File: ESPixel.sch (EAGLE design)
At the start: 15 parts, among them Q1 MOSFET-NCHANNEL2N7000

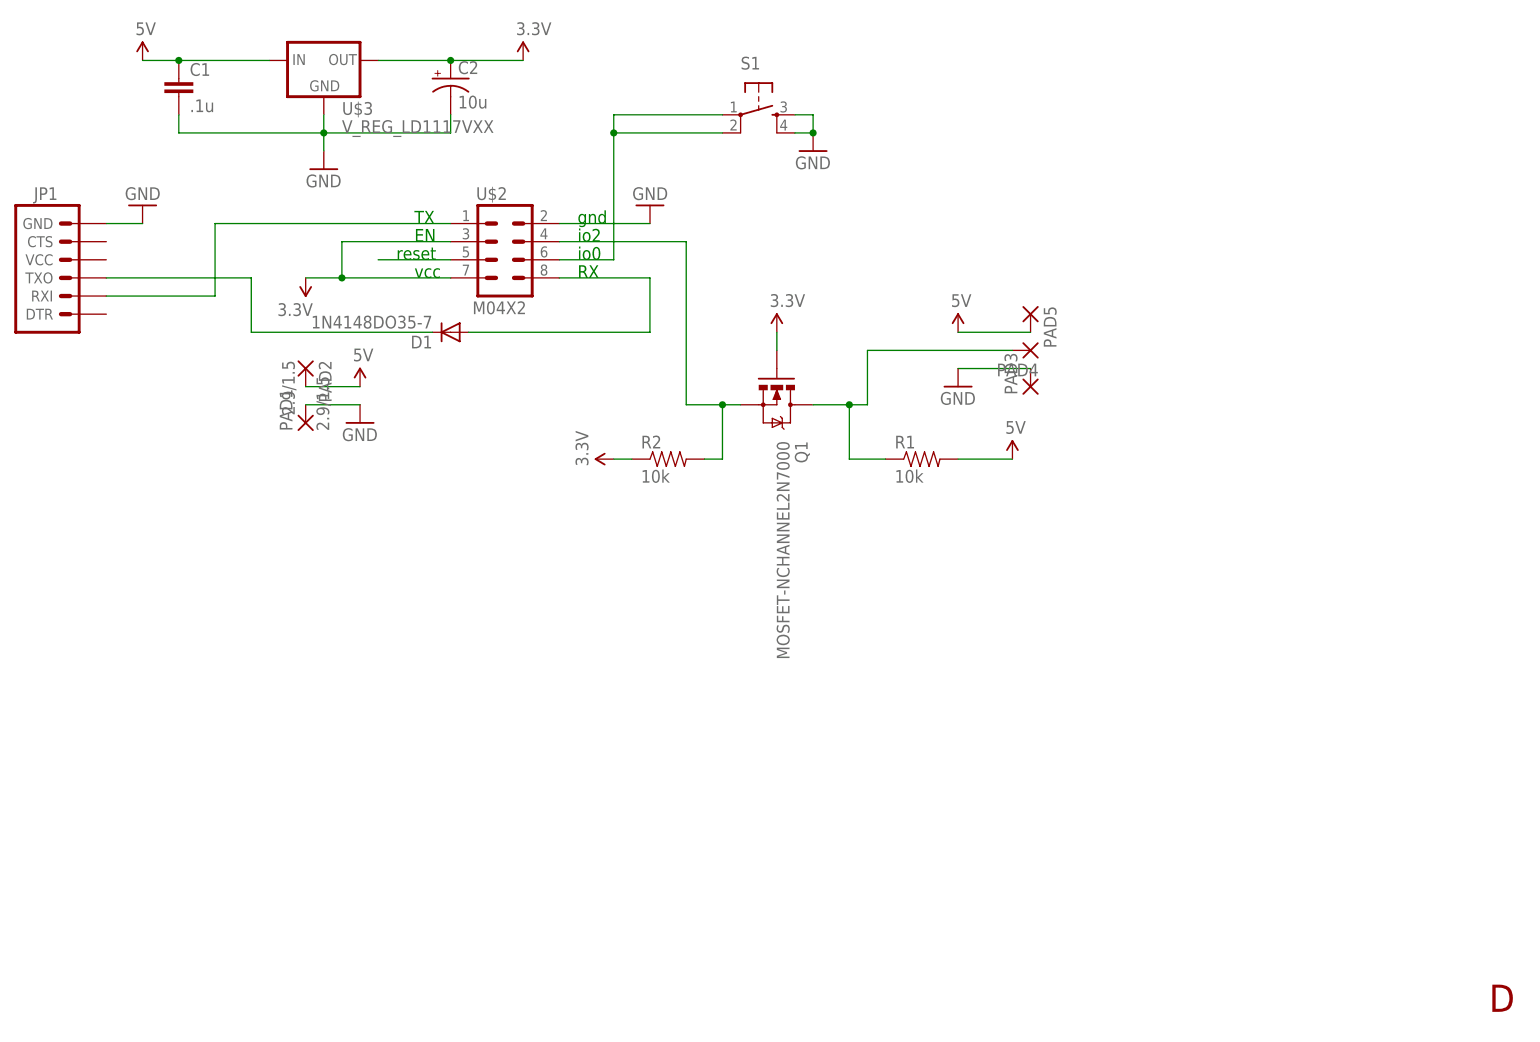
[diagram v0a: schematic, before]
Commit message: Added Diode to GECE and added WS2811 version
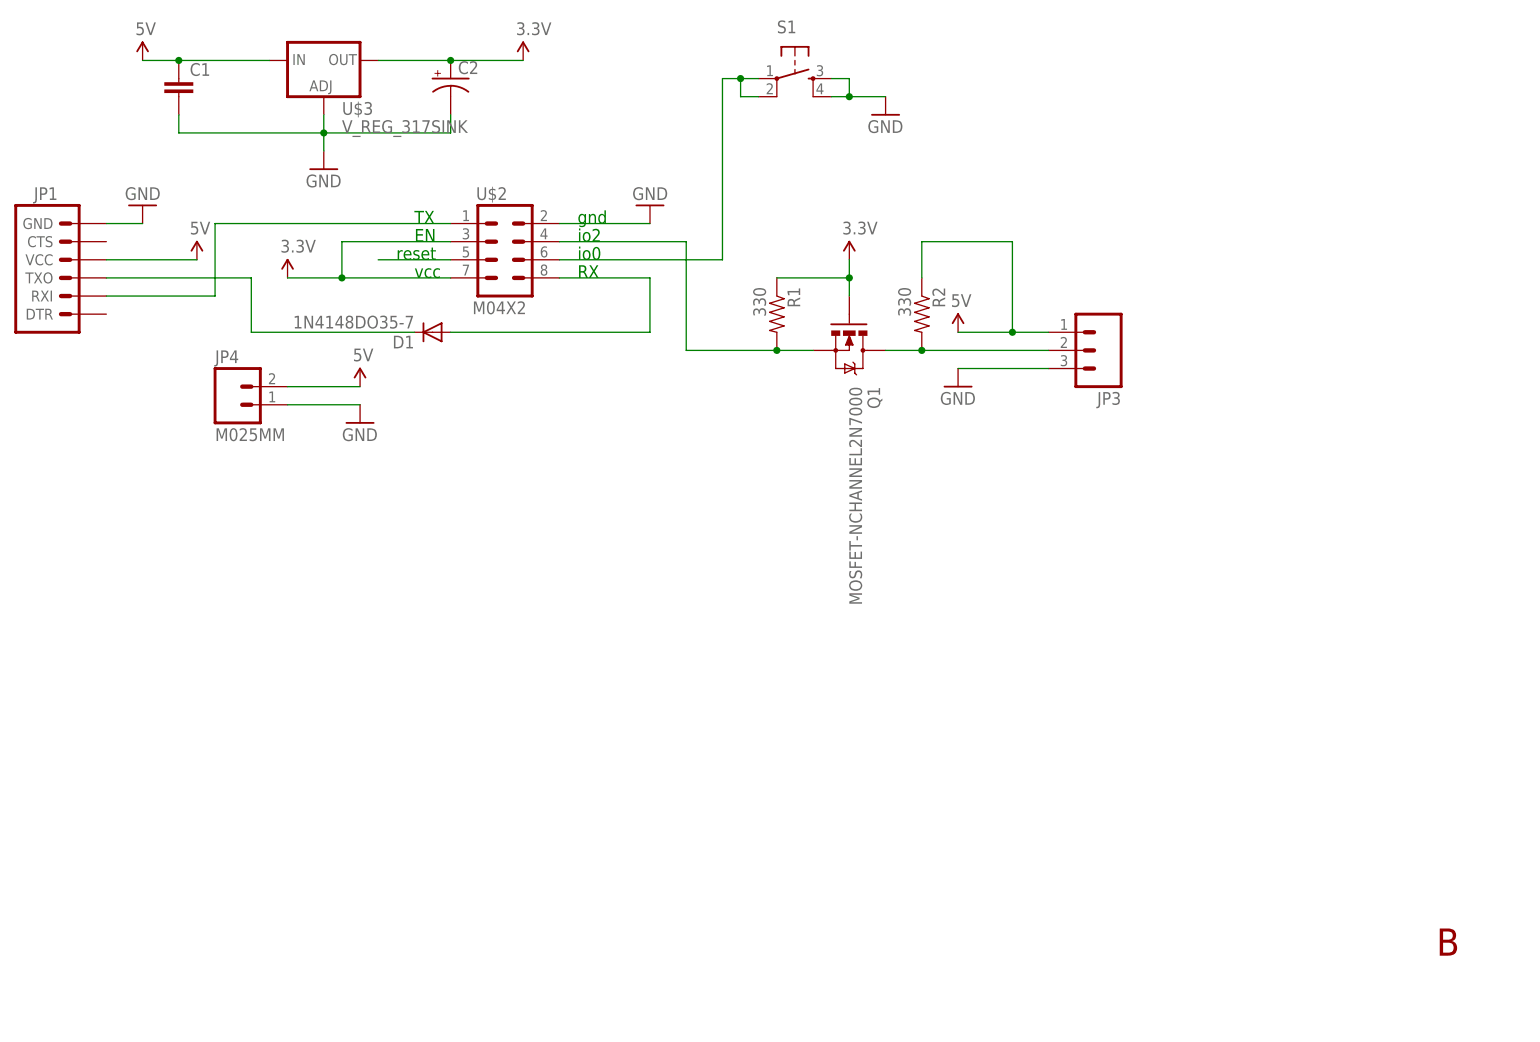
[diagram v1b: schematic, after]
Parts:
- removed PAD1, PAD2: 2.9/1.5, wirepad:2.9/1.5
- removed PAD3, PAD4, PAD5: (no value), wirepad:2,15/1,0
- added JP3: (no value), SparkFun-Connectors:M03-SCREW-5MM
- added JP4: M025MM, SparkFun-Connectors:M025MM
- C1: value .1u -> (none)
- C2: value 10u -> (none)
- R1, R2: value 10k -> 330
- U$3: value V_REG_LD1117VXX -> V_REG_317SINK; device SparkFun-PowerIC:V_REG_LD1117VXX -> SparkFun-PowerIC:V_REG_317SINK
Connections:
- net 3.3V: now also R1.1; no longer R2.1
- net 5V: now also JP1.VCC, JP3.1, JP4.2, R2.1; no longer PAD2.P, PAD5.P, R1.2
- net GND: now also JP3.3, JP4.1, U$3.ADJ; no longer PAD1.P, PAD3.P, U$3.GND
- net N$4: now also JP3.2, R2.2; no longer PAD4.P, R1.1
- net N$6: now also R1.2; no longer R2.2
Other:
- note added: "B"
- note removed: "D"
- moved on the sheet: D1, Q1, R1, R2, S1

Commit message: ESPixel now 12V or 5V
Added 5V reg for 12V pixel operation.
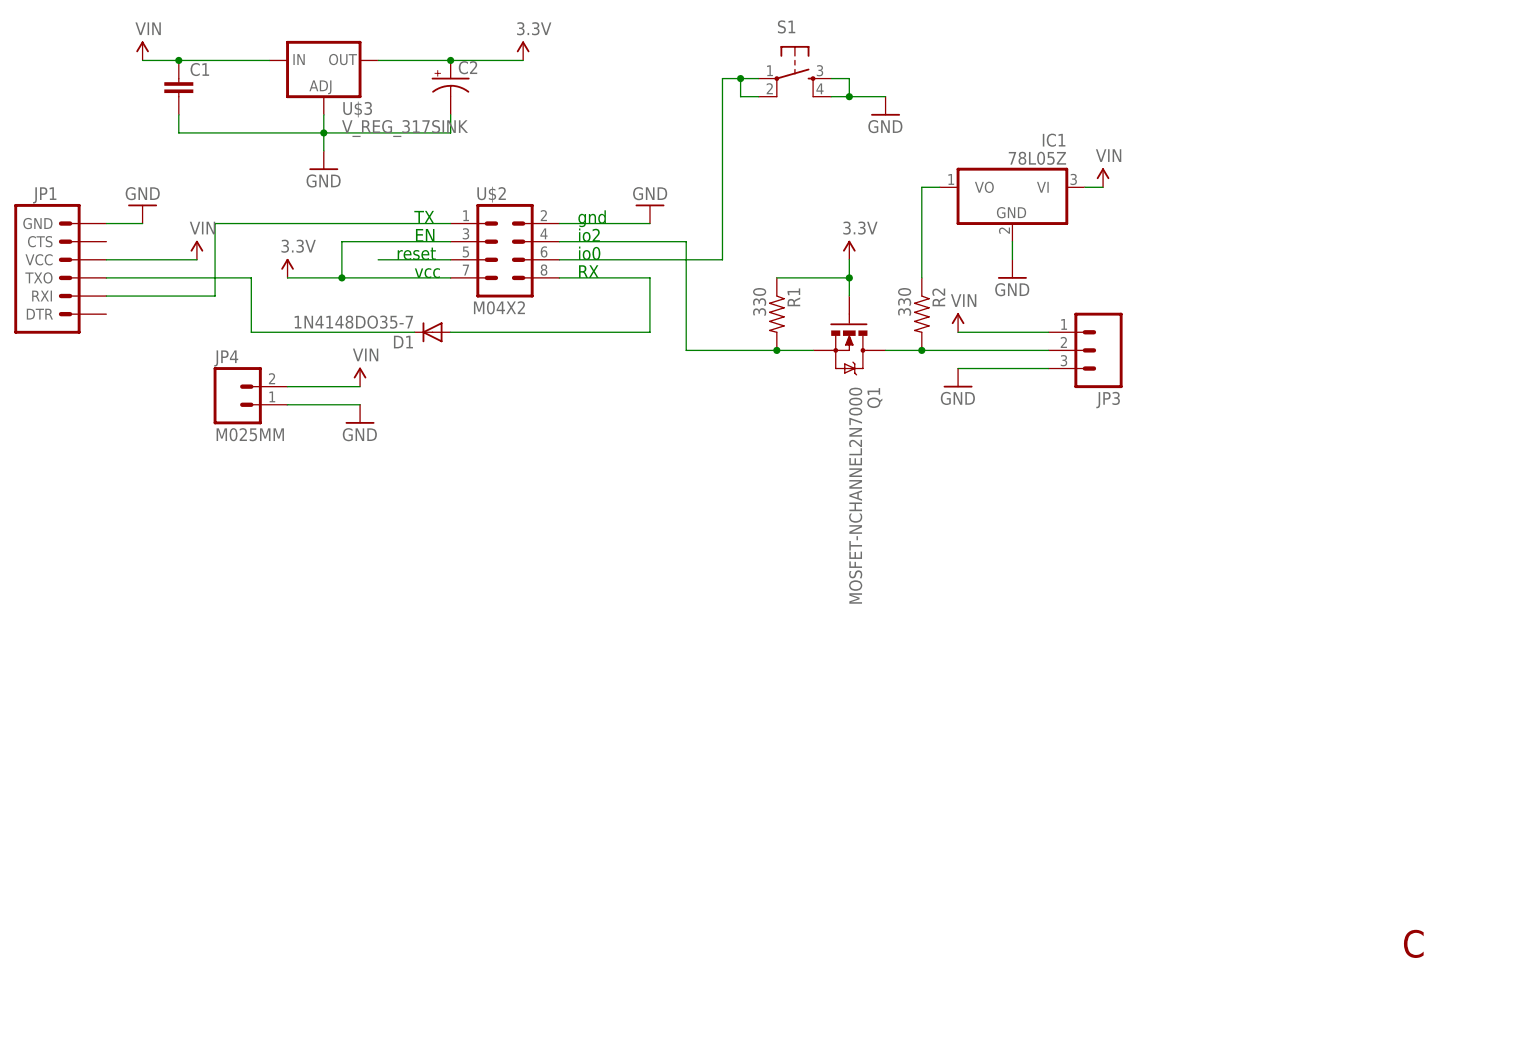
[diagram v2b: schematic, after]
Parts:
- added IC1: 78L05Z, linear:78L05Z
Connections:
- removed net 5V: C1.1, JP1.VCC, JP3.1, JP4.2, R2.1, U$3.IN
- new net N$2: IC1.VO, R2.1
- new net VIN: C1.1, IC1.VI, JP1.VCC, JP3.1, JP4.2, U$3.IN
- net GND: now also IC1.GND
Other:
- note added: "C"
- note removed: "B"
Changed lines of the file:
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@@
 <?xml version="1.0" encoding="utf-8"?>
 <!DOCTYPE eagle SYSTEM "eagle.dtd">
-<eagle version="7.2.0">
+<eagle version="7.4.0">
 <drawing>
 <settings>
@@
 <part name="SUPPLY1" library="SparkFun-Aesthetics" deviceset="3.3V" device=""/>
 <part name="U$3" library="SparkFun-PowerIC" deviceset="V_REG_317" device="SINK"/>
-<part name="SUPPLY3" library="SparkFun-Aesthetics" deviceset="5V" device=""/>
 <part name="SUPPLY4" library="SparkFun-Aesthetics" deviceset="3.3V" device=""/>
 <part name="GND4" library="SparkFun-Aesthetics" deviceset="GND" device=""/>
 <part name="C1" library="SparkFun-Capacitors" deviceset="CAP" device="EZ"/>
 <part name="C2" library="SparkFun-Capacitors" deviceset="CAP_POL" device="PTH2"/>
-<part name="SUPPLY5" library="SparkFun-Aesthetics" deviceset="5V" device=""/>
 <part name="SUPPLY2" library="SparkFun-Aesthetics" deviceset="3.3V" device=""/>
 <part name="R1" library="SparkFun-Resistors" deviceset="RESISTOR" device="EZ" value="330"/>
 <part name="JP3" library="SparkFun-Connectors" deviceset="M03" device="-SCREW-5MM"/>
 <part name="JP4" library="SparkFun-Connectors" deviceset="M02" device="5MM"/>
-<part name="SUPPLY7" library="SparkFun-Aesthetics" deviceset="5V" device=""/>
 <part name="GND2" library="SparkFun-Aesthetics" deviceset="GND" device=""/>
 <part name="GND5" library="SparkFun-Aesthetics" deviceset="GND" device=""/>
-<part name="SUPPLY8" library="SparkFun-Aesthetics" deviceset="5V" device=""/>
 <part name="S1" library="SparkFun-Retired" deviceset="TAC_SWITCH" device="PTH"/>
 <part name="GND6" library="SparkFun-Aesthetics" deviceset="GND" device=""/>
@@
 <part name="D1" library="diode" deviceset="1N4148" device="DO35-7"/>
 <part name="FRAME1" library="frames" deviceset="LETTER_L" device=""/>
+<part name="SUPPLY3" library="SparkFun-Aesthetics" deviceset="VIN" device=""/>
+<part name="SUPPLY5" library="SparkFun-Aesthetics" deviceset="VIN" device=""/>
+<part name="SUPPLY6" library="SparkFun-Aesthetics" deviceset="VIN" device=""/>
+<part name="SUPPLY7" library="SparkFun-Aesthetics" deviceset="VIN" device=""/>
+<part name="IC1" library="linear" deviceset="78*" device="Z" technology="L05"/>
+<part name="GND7" library="SparkFun-Aesthetics" deviceset="GND" device=""/>
+<part name="SUPPLY8" library="SparkFun-Aesthetics" deviceset="VIN" device=""/>
 </parts>
 <sheets>
@@
 <text x="91.44" y="91.44" size="1.778" layer="91">io0</text>
 <text x="91.44" y="88.9" size="1.778" layer="91">RX</text>
-<text x="211.836" y="-6.096" size="3.81" layer="94">B</text>
+<text x="207.01" y="-6.35" size="3.81" layer="94">C</text>
 </plain>
 <instances>
@@
 <instance part="SUPPLY1" gate="G$1" x="50.8" y="88.9"/>
 <instance part="U$3" gate="G$1" x="55.88" y="119.38"/>
-<instance part="SUPPLY3" gate="G$1" x="30.48" y="119.38"/>
 <instance part="SUPPLY4" gate="G$1" x="83.82" y="119.38"/>
 <instance part="GND4" gate="1" x="55.88" y="104.14"/>
 <instance part="C1" gate="G$1" x="35.56" y="114.3"/>
 <instance part="C2" gate="G$1" x="73.66" y="116.84"/>
-<instance part="SUPPLY5" gate="G$1" x="38.1" y="91.44"/>
 <instance part="SUPPLY2" gate="G$1" x="129.54" y="91.44"/>
 <instance part="R1" gate="G$1" x="119.38" y="83.82" rot="R270"/>
 <instance part="JP3" gate="G$1" x="165.1" y="78.74" rot="R180"/>
 <instance part="JP4" gate="G$1" x="43.18" y="71.12"/>
-<instance part="SUPPLY7" gate="G$1" x="60.96" y="73.66"/>
 <instance part="GND2" gate="1" x="60.96" y="68.58"/>
 <instance part="GND5" gate="1" x="144.78" y="73.66"/>
-<instance part="SUPPLY8" gate="G$1" x="144.78" y="81.28"/>
 <instance part="S1" gate="S" x="121.92" y="116.84"/>
 <instance part="GND6" gate="1" x="134.62" y="111.76"/>
@@
 <instance part="FRAME1" gate="G$1" x="-33.02" y="-12.7"/>
 <instance part="FRAME1" gate="G$2" x="114.3" y="-12.7"/>
+<instance part="SUPPLY3" gate="G$1" x="144.78" y="81.28"/>
+<instance part="SUPPLY5" gate="G$1" x="30.48" y="119.38"/>
+<instance part="SUPPLY6" gate="G$1" x="38.1" y="91.44"/>
+<instance part="SUPPLY7" gate="G$1" x="60.96" y="73.66"/>
+<instance part="IC1" gate="A1" x="152.4" y="101.6" rot="MR0"/>
+<instance part="GND7" gate="1" x="152.4" y="88.9"/>
+<instance part="SUPPLY8" gate="G$1" x="165.1" y="101.6"/>
 </instances>
 <busses>
@@
 <junction x="129.54" y="114.3"/>
 </segment>
+<segment>
+<pinref part="IC1" gate="A1" pin="GND"/>
+<pinref part="GND7" gate="1" pin="GND"/>
+<wire x1="152.4" y1="91.44" x2="152.4" y2="93.98" width="0.1524" layer="91"/>
+</segment>
 </net>
 <net name="3.3V" class="1">
@@
 </segment>
 </net>
-<net name="5V" class="1">
-<segment>
-<pinref part="U$3" gate="G$1" pin="IN"/>
-<pinref part="SUPPLY3" gate="G$1" pin="5V"/>
-<wire x1="30.48" y1="119.38" x2="35.56" y2="119.38" width="0.1524" layer="91"/>
-<pinref part="C1" gate="G$1" pin="1"/>
-<wire x1="35.56" y1="119.38" x2="48.26" y2="119.38" width="0.1524" layer="91"/>
-<junction x="35.56" y="119.38"/>
-</segment>
-<segment>
-<pinref part="SUPPLY5" gate="G$1" pin="5V"/>
-<pinref part="JP1" gate="G$1" pin="VCC"/>
-<wire x1="38.1" y1="91.44" x2="25.4" y2="91.44" width="0.1524" layer="91"/>
-</segment>
-<segment>
-<pinref part="JP4" gate="G$1" pin="2"/>
-<pinref part="SUPPLY7" gate="G$1" pin="5V"/>
-<wire x1="60.96" y1="73.66" x2="50.8" y2="73.66" width="0.1524" layer="91"/>
-</segment>
-<segment>
-<pinref part="JP3" gate="G$1" pin="1"/>
-<pinref part="SUPPLY8" gate="G$1" pin="5V"/>
-<wire x1="144.78" y1="81.28" x2="152.4" y2="81.28" width="0.1524" layer="91"/>
-<pinref part="R2" gate="G$1" pin="1"/>
-<wire x1="152.4" y1="81.28" x2="157.48" y2="81.28" width="0.1524" layer="91"/>
-<wire x1="139.7" y1="88.9" x2="139.7" y2="93.98" width="0.1524" layer="91"/>
-<wire x1="139.7" y1="93.98" x2="152.4" y2="93.98" width="0.1524" layer="91"/>
-<wire x1="152.4" y1="93.98" x2="152.4" y2="81.28" width="0.1524" layer="91"/>
-<junction x="152.4" y="81.28"/>
-</segment>
-</net>
 <net name="N$4" class="0">
 <segment>
@@
 </segment>
 </net>
+<net name="N$2" class="1">
+<segment>
+<pinref part="R2" gate="G$1" pin="1"/>
+<pinref part="IC1" gate="A1" pin="VO"/>
+<wire x1="142.24" y1="101.6" x2="139.7" y2="101.6" width="0.1524" layer="91"/>
+<wire x1="139.7" y1="101.6" x2="139.7" y2="88.9" width="0.1524" layer="91"/>
+</segment>
+</net>
+<net name="VIN" class="1">
+<segment>
+<pinref part="JP3" gate="G$1" pin="1"/>
+<wire x1="144.78" y1="81.28" x2="157.48" y2="81.28" width="0.1524" layer="91"/>
+<pinref part="SUPPLY3" gate="G$1" pin="VIN"/>
+</segment>
+<segment>
+<pinref part="U$3" gate="G$1" pin="IN"/>
+<wire x1="30.48" y1="119.38" x2="35.56" y2="119.38" width="0.1524" layer="91"/>
+<pinref part="C1" gate="G$1" pin="1"/>
+<wire x1="35.56" y1="119.38" x2="48.26" y2="119.38" width="0.1524" layer="91"/>
+<junction x="35.56" y="119.38"/>
+<pinref part="SUPPLY5" gate="G$1" pin="VIN"/>
+</segment>
+<segment>
+<pinref part="JP1" gate="G$1" pin="VCC"/>
+<wire x1="38.1" y1="91.44" x2="25.4" y2="91.44" width="0.1524" layer="91"/>
+<pinref part="SUPPLY6" gate="G$1" pin="VIN"/>
+</segment>
+<segment>
+<pinref part="JP4" gate="G$1" pin="2"/>
+<wire x1="60.96" y1="73.66" x2="50.8" y2="73.66" width="0.1524" layer="91"/>
+<pinref part="SUPPLY7" gate="G$1" pin="VIN"/>
+</segment>
+<segment>
+<pinref part="IC1" gate="A1" pin="VI"/>
+<pinref part="SUPPLY8" gate="G$1" pin="VIN"/>
+<wire x1="165.1" y1="101.6" x2="162.56" y2="101.6" width="0.1524" layer="91"/>
+</segment>
+</net>
